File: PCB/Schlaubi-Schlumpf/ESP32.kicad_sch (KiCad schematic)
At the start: 17 parts, among them J4 Conn_01x02_Pin, J5 Conn_01x02_Pin, SW1 SW_Push, SW2 SW_Push, U2 ESP32-S3-MINI-1-N8

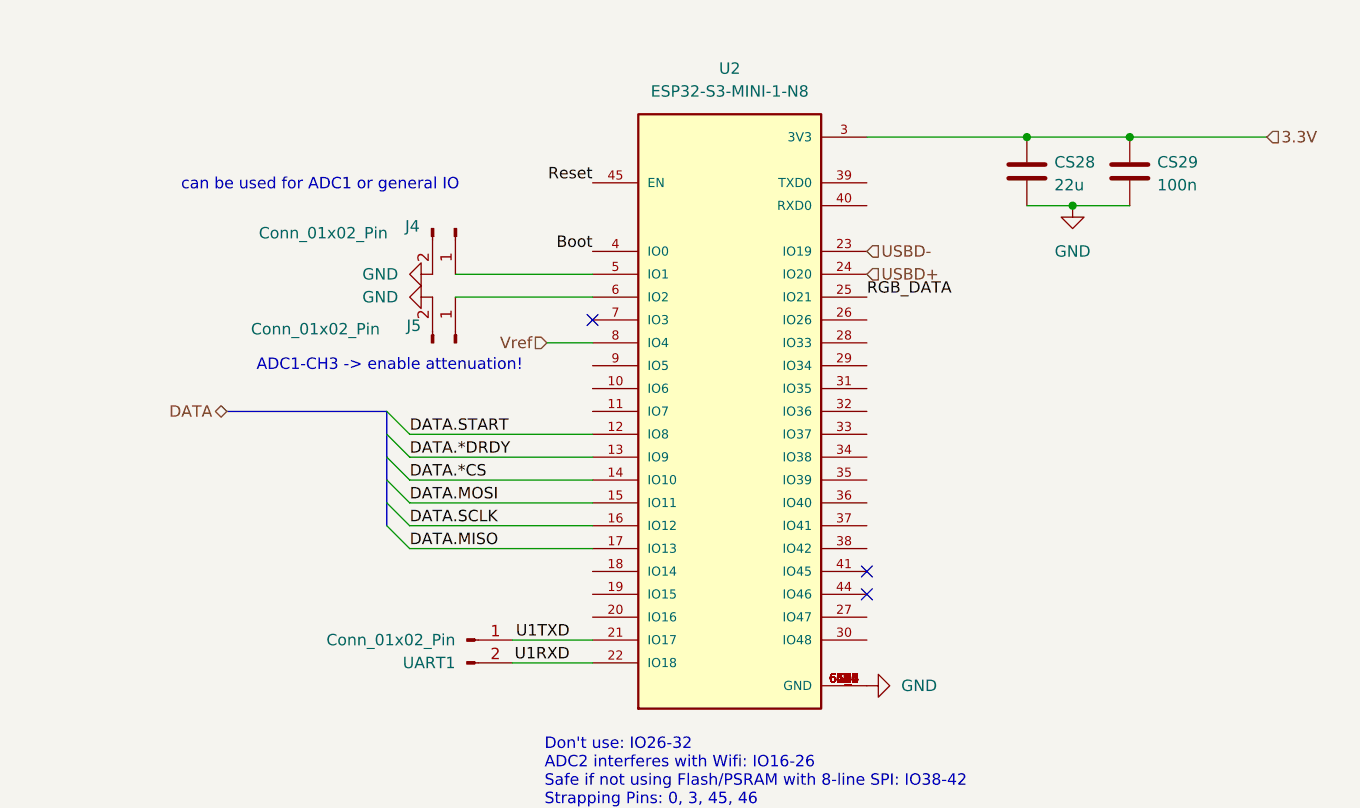
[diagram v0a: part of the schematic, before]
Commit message: added IMU
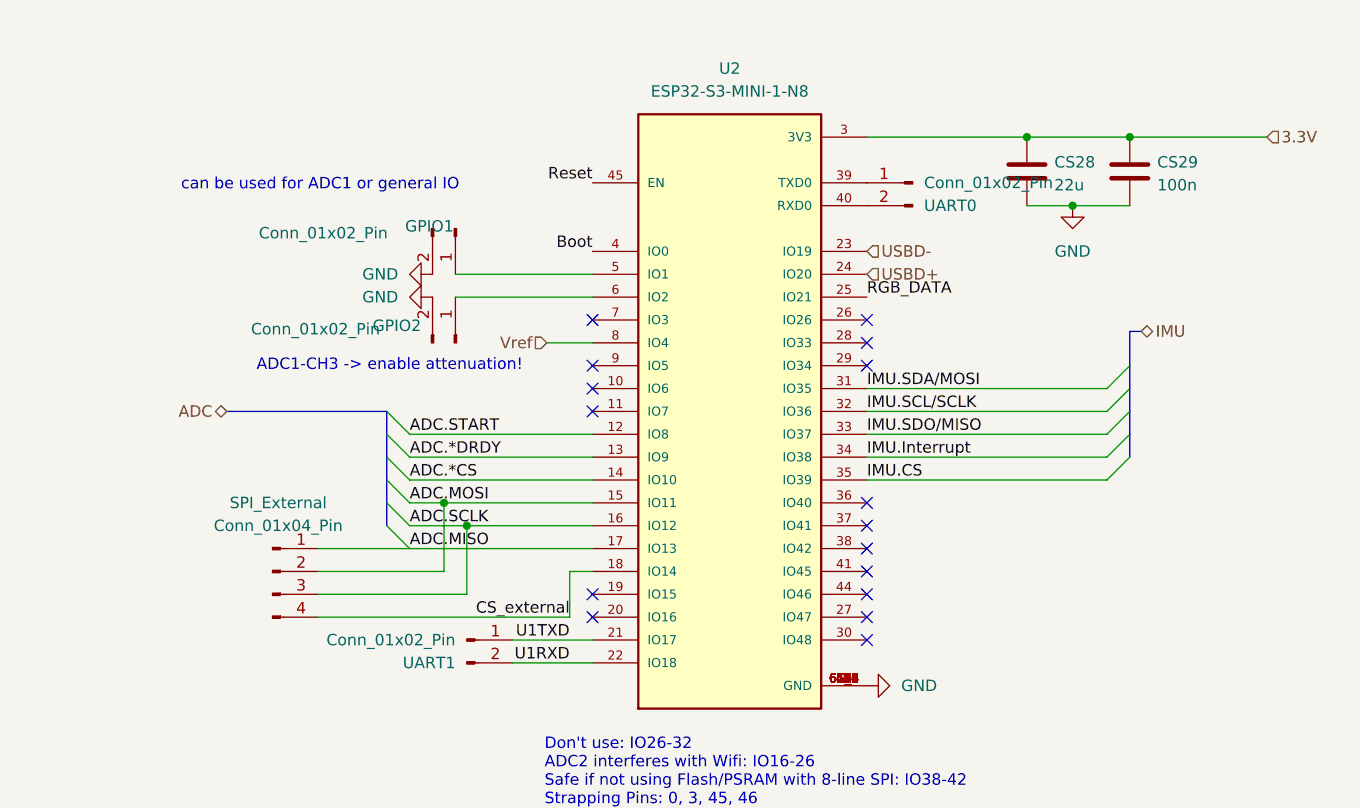
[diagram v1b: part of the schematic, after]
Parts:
- added SPI_External: Conn_01x04_Pin, symbol Connector:Conn_01x04_Pin
- added UART0: Conn_01x02_Pin, symbol Connector:Conn_01x02_Pin
- renumbered J4 to GPIO1, J5 to GPIO2
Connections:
- net CS_external: now reaches U2.18 (IO14)
- net CS_external: now also SPI_External.4 (Pin_4)
- net IMU.SDA/MOSI: now reaches U2.31 (IO35)
- net IMU.SCL/SCLK: now reaches U2.32 (IO36)
- net IMU.SDO/MISO: now reaches U2.33 (IO37)
- net IMU.Interrupt: now reaches U2.34 (IO38)
- net IMU.CS: now reaches U2.35 (IO39)
- net at U2.39 (TXD0): now also UART0.1 (Pin_1)
- net at U2.40 (RXD0): now also UART0.2 (Pin_2)
- net DATA.*CS renamed ADC.*CS
- net DATA.*DRDY renamed ADC.*DRDY
- net DATA.MISO renamed ADC.MISO
- net ADC.MISO: now also SPI_External.1 (Pin_1)
- net DATA.MOSI renamed ADC.MOSI
- net ADC.MOSI: now also SPI_External.2 (Pin_2)
- net DATA.SCLK renamed ADC.SCLK
- net ADC.SCLK: now also SPI_External.3 (Pin_3)
- net DATA.START renamed ADC.START
- no-connect marks 4 -> 17

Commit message: v1
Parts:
- removed CS45: 10u, Capacitor_SMD:C_0603_1608Metric, symbol Device:C
- removed D7: SK6812MINI-HS, SK6812MNI-HS:SK6812MNI-HS, symbol SK6812MNI-HS:SK6812MINI-HS
- removed SPI_External: Conn_01x04_Pin, symbol Connector:Conn_01x04_Pin
- removed SW1, SW2: SW_Push, symbol Switch:SW_Push
- added R27, R28, R29, R30: 0R, Resistor_SMD:R_0603_1608Metric, symbol Device:R
- added S2, S3: SKRPABE010, SKRPABE010:SW_SKRPABE010, symbol SKRPABE010:SKRPABE010
- added SPIEXT1: Conn_01x04_Pin, Connector_PinHeader_1.00mm:PinHeader_1x04_P1.00mm_Vertical, symbol Connector:Conn_01x04_Pin
- GPIO2: renamed from GPIO1; footprint (none) -> Connector_PinHeader_1.00mm:PinHeader_1x02_P1.00mm_Vertical
- GPIO3: renamed from GPIO2; footprint (none) -> Connector_PinHeader_1.00mm:PinHeader_1x02_P1.00mm_Vertical
- UART0, UART1: footprint (none) -> Connector_PinHeader_1.00mm:PinHeader_1x02_P1.00mm_Vertical
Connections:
- net ADC.*CS: now also R30.1; no longer U2.14 (IO10)
- net ADC.MISO: now also R27.1; no longer U2.17 (IO13)
- net ADC.MOSI: now also R28.1; no longer U2.15 (IO11)
- net ADC.SCLK: now also R29.1; no longer U2.16 (IO12)
- net Boot: now also S2.3, S2.4
- net CS_external: now also U2.36 (IO40), SPIEXT1.4 (Pin_4); no longer U2.18 (IO14)
- net GND: now also S2.1, S2.2, S3.1, S3.2
- net IMU.SCL/SCLK: now also SPIEXT1.2 (Pin_2)
- net IMU.SDA/MOSI: now also SPIEXT1.1 (Pin_1)
- net IMU.SDO/MISO: now also SPIEXT1.3 (Pin_3)
- net Reset: now also S3.3, S3.4
- net ADC.*RESET: now reaches U2.11 (IO7)
- new net: R30.2, U2.14 (IO10)
- new net: R28.2, U2.15 (IO11)
- new net: R29.2, U2.16 (IO12)
- new net: R27.2, U2.17 (IO13)
- no-connect marks 17 -> 16
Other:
- moved on the sheet: R13, UART1

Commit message: updates
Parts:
- GPIO2, GPIO3, UART0, UART1: footprint Connector_PinHeader_1.00mm:PinHeader_1x02_P1.00mm_Vertical -> Connector_PinHeader_1.27mm:PinHeader_1x02_P1.27mm_Vertical
- SPIEXT1: footprint Connector_PinHeader_1.00mm:PinHeader_1x04_P1.00mm_Vertical -> Connector_PinHeader_1.27mm:PinHeader_1x04_P1.27mm_Vertical; now not fitted; now left out of the parts list
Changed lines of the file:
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@@
 			)
 		)
-		(property "Footprint" "Connector_PinHeader_1.00mm:PinHeader_1x02_P1.00mm_Vertical"
+		(property "Footprint" "Connector_PinHeader_1.27mm:PinHeader_1x02_P1.27mm_Vertical"
 			(at 107.95 76.2 0)
 			(effects
@@
 			)
 		)
-		(property "Footprint" "Connector_PinHeader_1.00mm:PinHeader_1x02_P1.00mm_Vertical"
+		(property "Footprint" "Connector_PinHeader_1.27mm:PinHeader_1x02_P1.27mm_Vertical"
 			(at 158.75 71.12 0)
 			(effects
@@
 			)
 		)
-		(property "Footprint" "Connector_PinHeader_1.00mm:PinHeader_1x02_P1.00mm_Vertical"
+		(property "Footprint" "Connector_PinHeader_1.27mm:PinHeader_1x02_P1.27mm_Vertical"
 			(at 107.95 88.9 0)
 			(effects
@@
 			)
 		)
-		(property "Footprint" "Connector_PinHeader_1.00mm:PinHeader_1x02_P1.00mm_Vertical"
+		(property "Footprint" "Connector_PinHeader_1.27mm:PinHeader_1x02_P1.27mm_Vertical"
 			(at 113.03 121.92 0)
 			(effects
@@
 		(unit 1)
 		(exclude_from_sim no)
-		(in_bom yes)
-		(on_board yes)
-		(dnp no)
+		(in_bom no)
+		(on_board yes)
+		(dnp yes)
 		(property "Reference" "SPIEXT1"
 			(at 184.15 117.475 0)
@@
 			)
 		)
-		(property "Footprint" "Connector_PinHeader_1.00mm:PinHeader_1x04_P1.00mm_Vertical"
+		(property "Footprint" "Connector_PinHeader_1.27mm:PinHeader_1x04_P1.27mm_Vertical"
 			(at 176.53 118.11 0)
 			(effects

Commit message: update Opamp
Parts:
- added TP_CS1, TP_GND3, TP_MISO1, TP_MOSI1, TP_SCLK1: TestPoint, TestPoint:TestPoint_Pad_D1.0mm, symbol Connector:TestPoint
- SPIEXT1: now fitted; now in the parts list
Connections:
- net ADC.*CS: now also TP_CS1.1
- net ADC.MOSI: now also TP_MOSI1.1
- net ADC.SCLK: now also TP_SCLK1.1
- net GND: now also TP_GND3.1
- net ADC.*PWDN: now reaches U2.10 (IO6)
- net at R27.2, U2.17 (IO13): now also TP_MISO1.1
- net Vref: no longer names the net of U2.8 (IO4)
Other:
- note removed: "ADC1-CH3 -> enable attenuation!"

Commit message: newest order 17.09
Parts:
- removed SPIEXT1: Conn_01x04_Pin, Connector_PinHeader_1.27mm:PinHeader_1x04_P1.27mm_Vertical, symbol Connector:Conn_01x04_Pin
- added CS_External1: TestPoint, TestPoint:TestPoint_THTPad_D1.0mm_Drill0.5mm, symbol Connector:TestPoint
- added TP_DRDY1: TestPoint, TestPoint:TestPoint_Pad_D1.0mm, symbol Connector:TestPoint
- R27: value 0R -> 27R
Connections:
- net ADC.*DRDY: now also TP_DRDY1.1
- net CS_external: now also CS_External1.1
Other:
- note added: "Ideally set *Reset and *PWDN High for normal Operation"
- note added: "Set *RESET & *PWDN typically high"
